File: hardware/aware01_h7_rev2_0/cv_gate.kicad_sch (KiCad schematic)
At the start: 44 parts, among them J1 CV3_IN, J10 CV2_IN, J11 V/OCT_IN, J12 CV1_IN, J13 GATE3_IN, J14 GATE4_IN, J8 GATE1_IN, J9 GATE2_IN, Q1 MMBT3904, Q2 MMBT3904, Q3 MMBT3904, Q4 MMBT3904, U11 LMV722IDR, U12 LMV722IDR

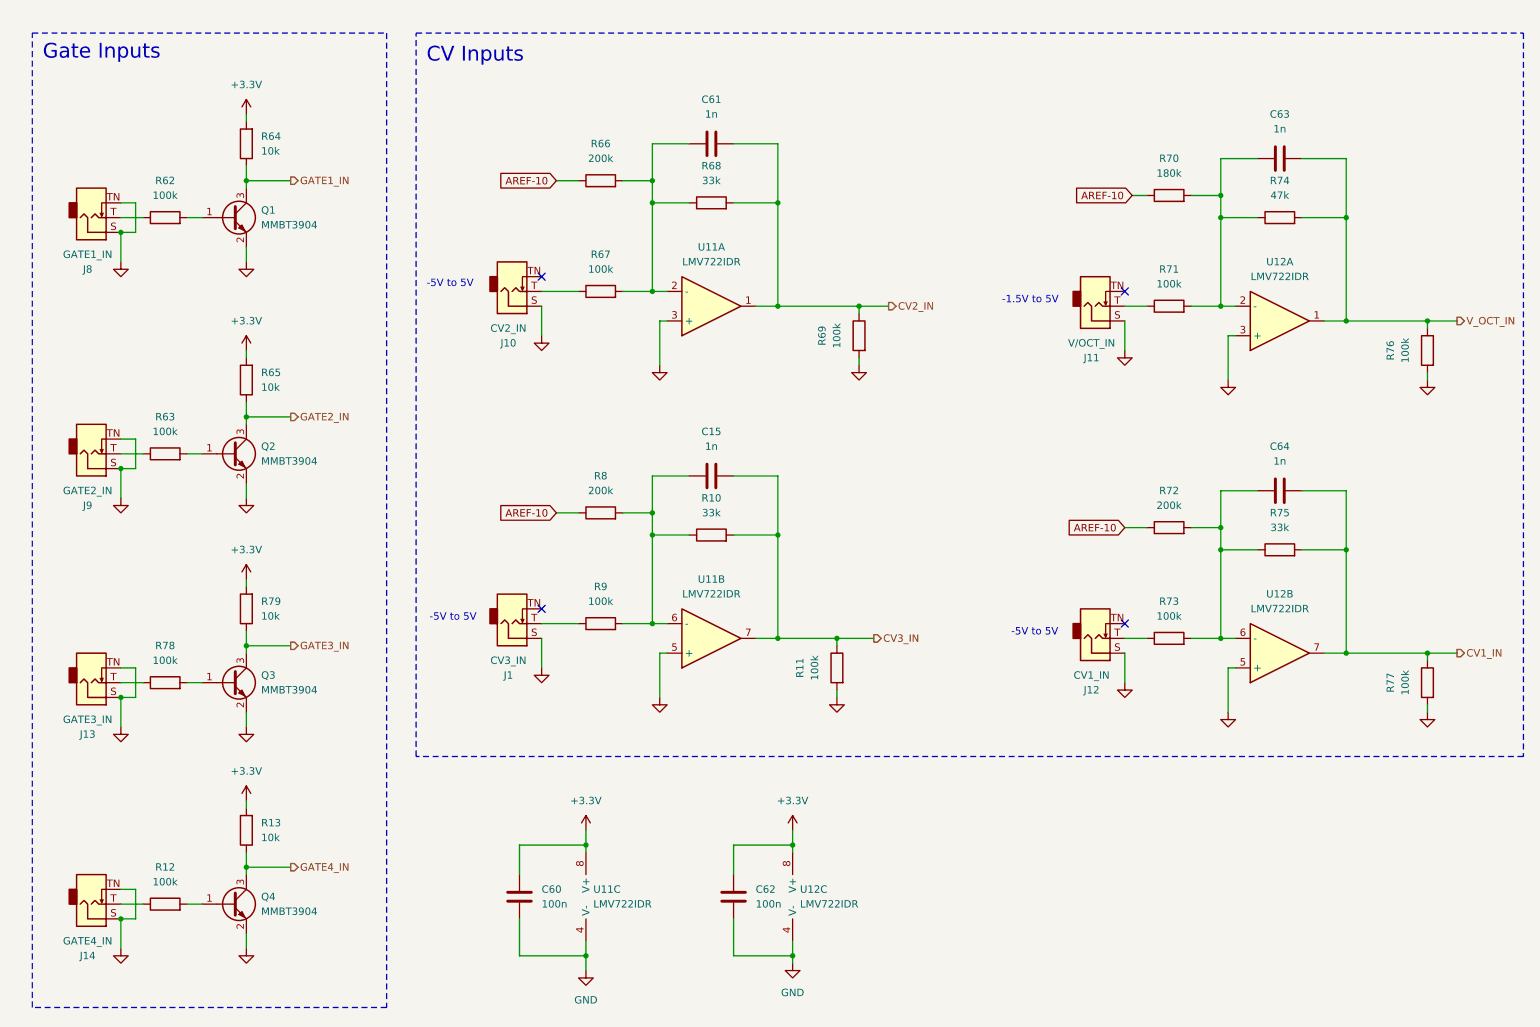
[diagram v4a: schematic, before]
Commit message: hwardware: update analog stages simulation
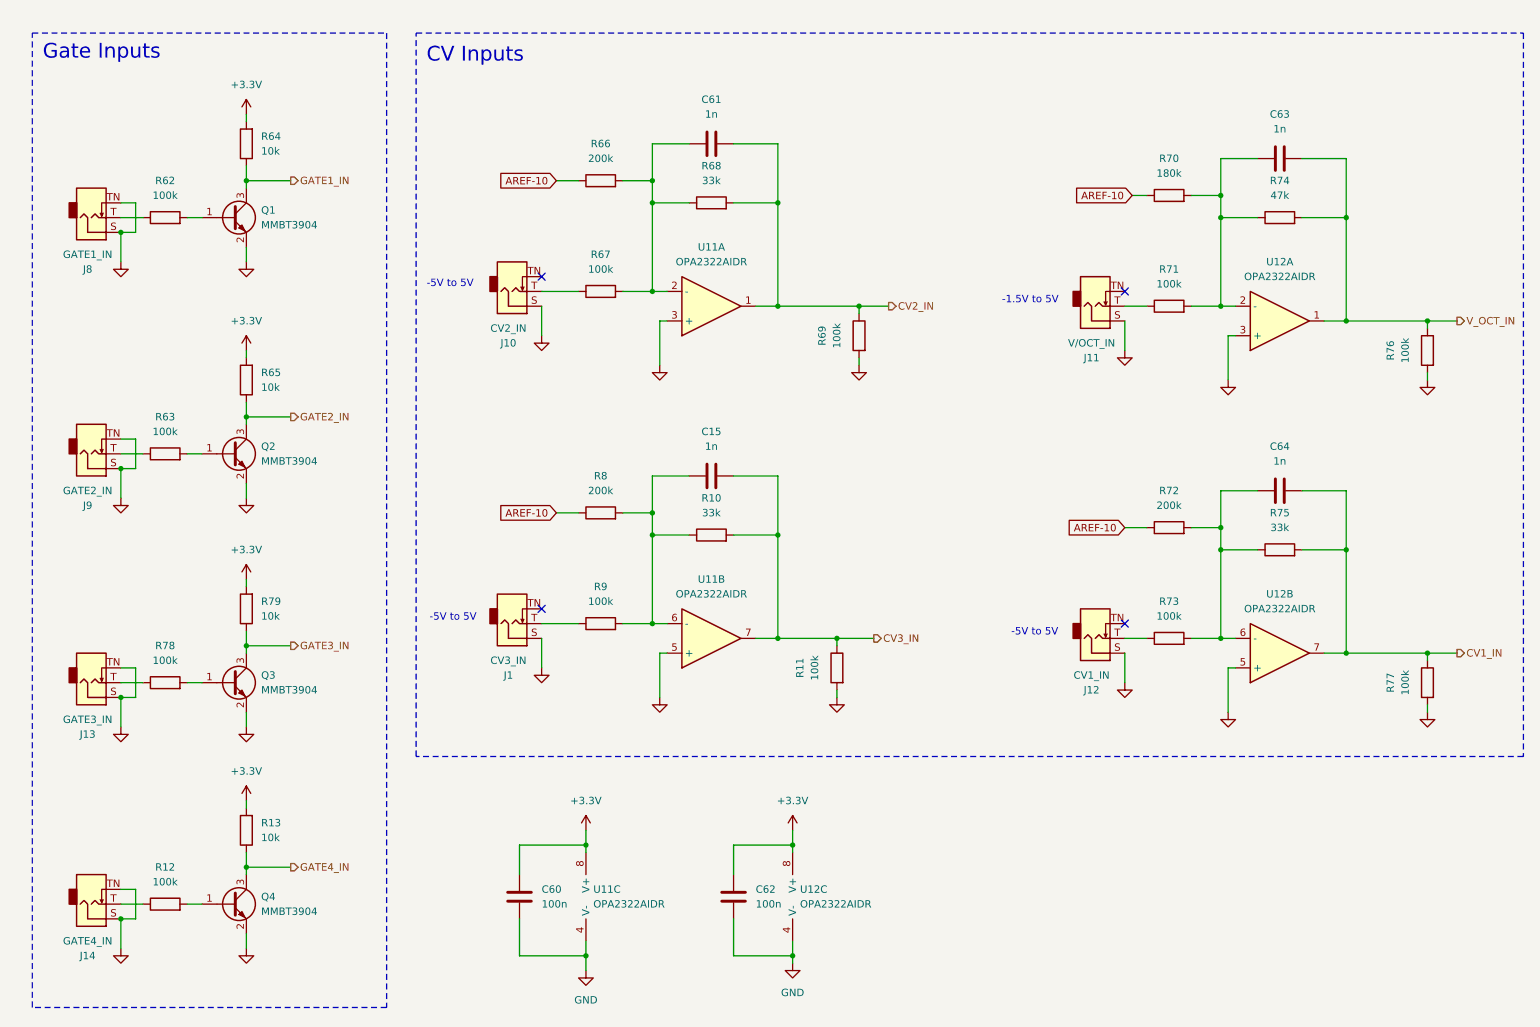
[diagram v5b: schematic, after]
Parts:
- U11, U12: value LMV722IDR -> OPA2322AIDR; footprint Eurorack:LMV722IDR -> Package_SO:SOIC-8_3.9x4.9mm_P1.27mm; Manufacturer_Part_Number LMV722IDR -> OPA2322AIDR; Mouser Part Number 595-LMV722IDR -> 595-OPA2322AIDR
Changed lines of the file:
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@@
 			)
 		)
-		(property "Value" "LMV722IDR"
+		(property "Value" "OPA2322AIDR"
 			(at 137.16 59.69 0)
 			(effects
@@
 			)
 		)
-		(property "Footprint" "Eurorack:LMV722IDR"
+		(property "Footprint" "Package_SO:SOIC-8_3.9x4.9mm_P1.27mm"
 			(at 137.16 67.31 0)
 			(effects
@@
 			)
 		)
-		(property "Datasheet" "~"
+		(property "Datasheet" "https://www.ti.com/lit/ds/symlink/opa2322.pdf?ts=1763625919584"
 			(at 137.16 67.31 0)
 			(effects
@@
 			)
 		)
-		(property "Manufacturer_Part_Number" "LMV722IDR "
+		(property "Manufacturer_Part_Number" "OPA2322AIDR"
 			(at 137.16 67.31 0)
 			(effects
@@
 			)
 		)
-		(property "Mouser Part Number" " 595-LMV722IDR"
+		(property "Mouser Part Number" " 595-OPA2322AIDR"
 			(at 137.16 67.31 0)
 			(effects
@@
 			)
 		)
-		(property "Value" "LMV722IDR"
+		(property "Value" "OPA2322AIDR"
 			(at 116.84 170.1799 0)
 			(effects
@@
 			)
 		)
-		(property "Footprint" "Eurorack:LMV722IDR"
+		(property "Footprint" "Package_SO:SOIC-8_3.9x4.9mm_P1.27mm"
 			(at 118.11 168.91 0)
 			(effects
@@
 			)
 		)
-		(property "Datasheet" "~"
+		(property "Datasheet" "https://www.ti.com/lit/ds/symlink/opa2322.pdf?ts=1763625919584"
 			(at 118.11 168.91 0)
 			(effects
@@
 			)
 		)
-		(property "Manufacturer_Part_Number" "LMV722IDR "
+		(property "Manufacturer_Part_Number" "OPA2322AIDR"
 			(at 118.11 168.91 0)
 			(effects
@@
 			)
 		)
-		(property "Mouser Part Number" " 595-LMV722IDR"
+		(property "Mouser Part Number" " 595-OPA2322AIDR"
 			(at 118.11 168.91 0)
 			(effects
@@
 			)
 		)
-		(property "Value" "LMV722IDR"
+		(property "Value" "OPA2322AIDR"
 			(at 137.16 116.84 0)
 			(effects
@@
 			)
 		)
-		(property "Footprint" "Eurorack:LMV722IDR"
+		(property "Footprint" "Package_SO:SOIC-8_3.9x4.9mm_P1.27mm"
 			(at 137.16 124.46 0)
 			(effects
@@
 			)
 		)
-		(property "Datasheet" "~"
+		(property "Datasheet" "https://www.ti.com/lit/ds/symlink/opa2322.pdf?ts=1763625919584"
 			(at 137.16 124.46 0)
 			(effects
@@
 			)
 		)
-		(property "Manufacturer_Part_Number" "LMV722IDR "
+		(property "Manufacturer_Part_Number" "OPA2322AIDR"
 			(at 137.16 124.46 0)
 			(effects
@@
 			)
 		)
-		(property "Mouser Part Number" " 595-LMV722IDR"
+		(property "Mouser Part Number" " 595-OPA2322AIDR"
 			(at 137.16 124.46 0)
 			(effects
@@
 			)
 		)
-		(property "Value" "LMV722IDR"
+		(property "Value" "OPA2322AIDR"
 			(at 152.4 170.1799 0)
 			(effects
@@
 			)
 		)
-		(property "Footprint" "Eurorack:LMV722IDR"
+		(property "Footprint" "Package_SO:SOIC-8_3.9x4.9mm_P1.27mm"
 			(at 153.67 168.91 0)
 			(effects
@@
 			)
 		)
-		(property "Datasheet" "~"
+		(property "Datasheet" "https://www.ti.com/lit/ds/symlink/opa2322.pdf?ts=1763625919584"
 			(at 153.67 168.91 0)
 			(effects
@@
 			)
 		)
-		(property "Manufacturer_Part_Number" "LMV722IDR "
+		(property "Manufacturer_Part_Number" "OPA2322AIDR"
 			(at 153.67 168.91 0)
 			(effects
@@
 			)
 		)
-		(property "Mouser Part Number" " 595-LMV722IDR"
+		(property "Mouser Part Number" " 595-OPA2322AIDR"
 			(at 153.67 168.91 0)
 			(effects
@@
 			)
 		)
-		(property "Value" "LMV722IDR"
+		(property "Value" "OPA2322AIDR"
 			(at 234.95 62.23 0)
 			(effects
@@
 			)
 		)
-		(property "Footprint" "Eurorack:LMV722IDR"
+		(property "Footprint" "Package_SO:SOIC-8_3.9x4.9mm_P1.27mm"
 			(at 234.95 69.85 0)
 			(effects
@@
 			)
 		)
-		(property "Datasheet" "~"
+		(property "Datasheet" "https://www.ti.com/lit/ds/symlink/opa2322.pdf?ts=1763625919584"
 			(at 234.95 69.85 0)
 			(effects
@@
 			)
 		)
-		(property "Manufacturer_Part_Number" "LMV722IDR "
+		(property "Manufacturer_Part_Number" "OPA2322AIDR"
 			(at 234.95 69.85 0)
 			(effects
@@
 			)
 		)
-		(property "Mouser Part Number" " 595-LMV722IDR"
+		(property "Mouser Part Number" " 595-OPA2322AIDR"
 			(at 234.95 69.85 0)
 			(effects
@@
 			)
 		)
-		(property "Value" "LMV722IDR"
+		(property "Value" "OPA2322AIDR"
 			(at 234.95 119.38 0)
 			(effects
@@
 			)
 		)
-		(property "Footprint" "Eurorack:LMV722IDR"
+		(property "Footprint" "Package_SO:SOIC-8_3.9x4.9mm_P1.27mm"
 			(at 234.95 127 0)
 			(effects
@@
 			)
 		)
-		(property "Datasheet" "~"
+		(property "Datasheet" "https://www.ti.com/lit/ds/symlink/opa2322.pdf?ts=1763625919584"
 			(at 234.95 127 0)
 			(effects
@@
 			)
 		)
-		(property "Manufacturer_Part_Number" "LMV722IDR "
+		(property "Manufacturer_Part_Number" "OPA2322AIDR"
 			(at 234.95 127 0)
 			(effects
@@
 			)
 		)
-		(property "Mouser Part Number" " 595-LMV722IDR"
+		(property "Mouser Part Number" " 595-OPA2322AIDR"
 			(at 234.95 127 0)
 			(effects

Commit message: hardware: update analog sim and routing (wip)
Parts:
- removed R11, R69, R76, R77: 100k, Resistor_SMD:R_0603_1608Metric_Pad0.98x0.95mm_HandSolder, symbol Device:R
- added D6, D7: BAT54A, Package_TO_SOT_SMD:SOT-23, symbol Diode:BAT54A
- renumbered C60 to C56, C61 to C57, C15 to C58, C62 to C59, C63 to C60, C64 to C61, J14 to J10, J10 to J11, J1 to J12, J11 to J13, J12 to J14, J8 to J7, J9 to J8, J13 to J9, R62 to R24, R63 to R25, R78 to R26, R12 to R27, R64 to R28, R65 to R29, R79 to R30, R13 to R31, R66 to R32, R67 to R33, R8 to R34, R9 to R35, R68 to R36, R10 to R37, R70 to R38, R71 to R39, R72 to R40, R73 to R41, R74 to R42, R75 to R43, U11 to U12, U12 to U13
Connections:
- net GND: now also D6.3, D7.3
- net at Q2.1 (B), R25.2: now also D6.2
- net at Q1.1 (B), R24.2: now also D6.1
- net at Q3.1 (B), R26.2: now also D7.1
- net at Q4.1 (B), R27.2: now also D7.2

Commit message: hardware: update layout
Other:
- company: (none) -> Ausschussware
- title: (none) -> Aware 01 - Eurorack DSP Module
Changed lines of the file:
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@@
 	(generator_version "9.0")
 	(paper "A4")
+	(title_block
+		(title "Aware 01 - Eurorack DSP Module")
+		(date "2025-12-19")
+		(rev "2")
+		(company "Ausschussware")
+		(comment 1 "Jonas Bengt Lux")
+		(comment 2 "TH Köln")
+		(comment 3 "Bachelor Technische Informatik")
+	)
 	(rectangle
 		(start 86.36 20.32)

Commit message: hw: improve layout, update BOM
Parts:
- D6, D7: Manufacturer_Name (none) -> Vishay Semiconductors; Manufacturer_Part_Number (none) -> BAT54A-E3-08; Mouser Part Number (none) -> 78-BAT54A-E3-08
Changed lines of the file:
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@@
+			)
+		)
+		(property "Manufacturer_Name" "Vishay Semiconductors "
+			(at 49.53 152.4 90)
+			(effects
+				(font
+					(size 1.27 1.27)
+				)
+				(hide yes)
+			)
+		)
+		(property "Manufacturer_Part_Number" " BAT54A-E3-08 "
+			(at 49.53 152.4 90)
+			(effects
+				(font
+					(size 1.27 1.27)
+				)
+				(hide yes)
+			)
+		)
+		(property "Mouser Part Number" " 78-BAT54A-E3-08 "
+			(at 49.53 152.4 90)
+			(effects
+				(font
+					(size 1.27 1.27)
+				)
+				(hide yes)
 			)
 		)
@@
 			(effects
 				(font
+					(size 1.27 1.27)
+				)
+				(hide yes)
+			)
+		)
+		(property "Manufacturer_Name" "Vishay Semiconductors "
+			(at 49.53 72.39 90)
+			(effects
+				(font
+					(size 1.27 1.27)
+				)
+				(hide yes)
+			)
+		)
+		(property "Manufacturer_Part_Number" " BAT54A-E3-08 "
+			(at 49.53 72.39 90)
+			(effects
+				(font
+					(size 1.27 1.27)
+				)
+				(hide yes)
+			)
+		)
+		(property "Mouser Part Number" " 78-BAT54A-E3-08 "
+			(at 49.53 72.39 90)
+			(effects
+				(font
